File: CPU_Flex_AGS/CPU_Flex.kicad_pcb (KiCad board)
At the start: 2 copper layers, 20.5 x 21.3 mm, 4 parts, among them J3 Conn_01x16, J4 CPU_AGB_B_Interface

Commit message: updated CPU-flex
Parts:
- BAT+, GND: footprint TestPoint:TestPoint_Pad_D1.5mm -> TestPoint:TestPoint_THTPad_D1.5mm_Drill0.7mm
- J4: footprint Nintendo:CPU_AGB_B_Interface -> Ninteno:CPU_AGB_B_Interface
- moved GND 14.0 mm to (94.7, 87.3)
- moved BAT+ 10.5 mm to (94.7, 92.7)
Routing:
- net VCC: track 21.5 -> 36.1 mm, vias 0 -> 2
- net GND: track 17.3 -> 5.40 mm, vias 0 -> 8
- net /GBA_R: track 23.1 -> 27.6 mm
- net /GBA_B: track 24.5 -> 28.7 mm, vias 1 -> 2
- net /GBA_AUD_L: track 26.5 -> 29.0 mm, vias 1 -> 0
- net /GBA_A: track 23.2 -> 25.1 mm
- net /GBA_RESET: track 22.4 -> 23.5 mm
- net /GBA_AUD_R: track 27.8 -> 28.7 mm
- added copper zone on B.Cu, net GND
- added copper zone on F.Cu, net GND
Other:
- board size 20.5 x 21.3 mm -> 23.4 x 20.4 mm
- net class Default removed
- board text added: "CPU AGB B-Flex PCB"
- board text added: "by ManCloud"
- board text added: "for gbaHD"
- board text added: "v20211229"

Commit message: updated CPU-FLEX
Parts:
- J4: value CPU_AGB_B_Interface -> CPU AGB B Interface
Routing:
- net GND: track 5.40 -> 2.11 mm, vias 8 -> 14
- net /GBA_R: track 27.6 -> 28.7 mm
- net /GBA_B: track 28.7 -> 29.7 mm
- net /GBA_CLK: track 19.1 -> 20.0 mm
- net /GBA_UP: track 10.6 -> 11.5 mm
- net /GBA_SELECT: track 18.7 -> 19.5 mm
- net /GBA_DOWN: track 11.9 -> 12.7 mm
- net /GBA_AUD_L: track 29.0 -> 29.9 mm
- net /GBA_RESET: track 23.5 -> 24.2 mm
- net /GBA_RIGHT: track 13.2 -> 13.9 mm
- net /GBA_LEFT: track 11.9 -> 12.6 mm
- net /GBA_L: track 13.1 -> 13.8 mm
- net /GBA_AUD_R: track 28.7 -> 29.4 mm
- net /GBA_A: track 25.1 -> 25.7 mm
- net /GBA_START: track 17.8 -> 18.5 mm
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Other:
- outline, holes or cut-outs redrawn
- board text added: "v20220114"
- board text removed: "v20211229"

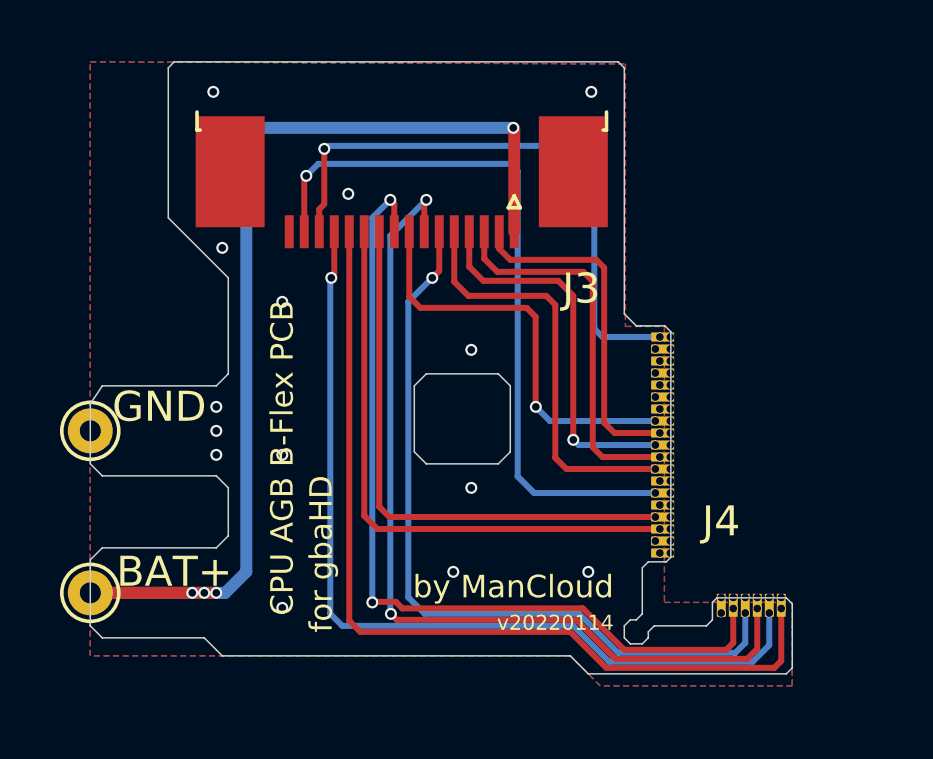
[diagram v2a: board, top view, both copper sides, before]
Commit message: Updated QSB for AGB/AGS CPU
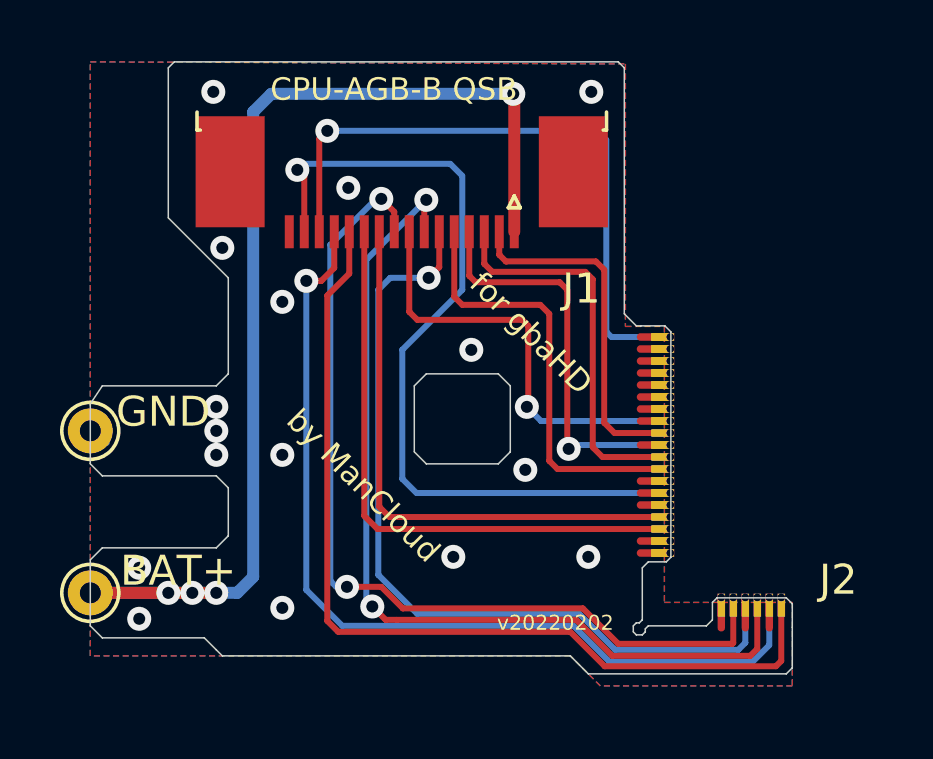
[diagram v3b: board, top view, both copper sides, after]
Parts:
- J2: renamed from J4; value CPU AGB B Interface -> CPU_AGB_B_Interface
- renumbered J3 to J1
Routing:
- net (no net): track 0.00 -> 11.0 mm
- net /GBA_RESET: track 24.2 -> 28.5 mm
- net /GBA_A: track 25.7 -> 28.7 mm
- net VCC: track 36.1 -> 38.4 mm
- net /GBA_CLK: track 20.0 -> 22.1 mm
- net /GBA_AUD_R: track 29.4 -> 31.4 mm
- net /GBA_LEFT: track 12.6 -> 14.2 mm
- net /GBA_R: track 28.7 -> 30.3 mm
- net /GBA_L: track 13.8 -> 15.0 mm
- net /GBA_AUD_L: track 29.9 -> 30.9 mm
- net /GBA_B: track 29.7 -> 30.5 mm
- net GND: vias 14 -> 16
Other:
- outline, holes or cut-outs redrawn
- rule pad_to_mask_clearance: 0 -> 0.0508
- board text added: "CPU-AGB-B QSB"
- board text added: "v20220202"
- board text removed: "CPU AGB B-Flex PCB"
- board text removed: "v20220114"

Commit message: Updated PCBs
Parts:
- J2: value CPU_AGB_B_Interface -> CPU AGB B Interface; footprint Ninteno:CPU_AGB_B_Interface -> Nintendo:CPU_AGB_B_Interface
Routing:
- net /GBA_R: track 30.3 -> 31.3 mm
- net /GBA_B: track 30.5 -> 31.5 mm
- net /GBA_AUD_L: track 30.9 -> 31.9 mm
- net (no net): track 11.0 -> 12.0 mm
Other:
- outline, holes or cut-outs redrawn
- board text added: "v20220310"
- board text removed: "v20220202"
